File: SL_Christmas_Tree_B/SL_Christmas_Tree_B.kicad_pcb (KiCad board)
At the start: 2 copper layers, 85.7 x 116 mm, 60 parts

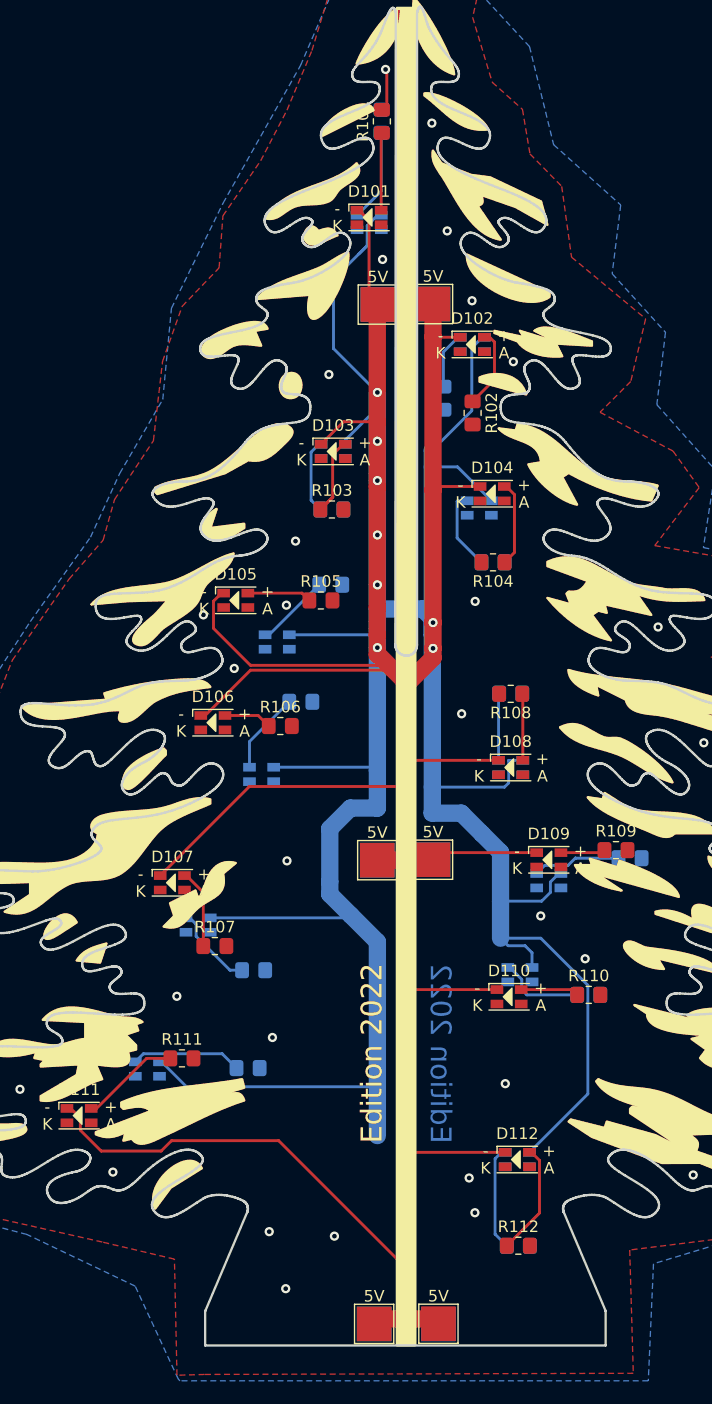
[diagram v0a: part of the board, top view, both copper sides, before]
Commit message: fix swapped 5V / GND
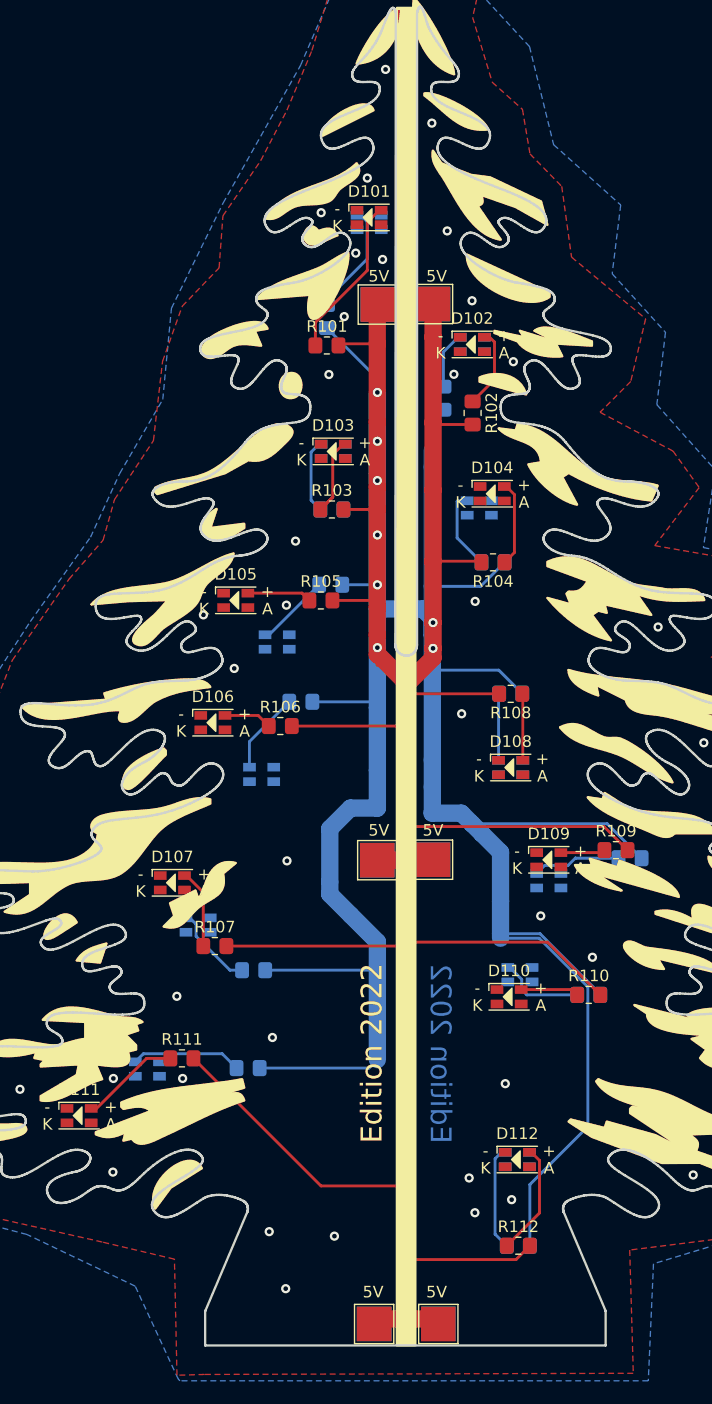
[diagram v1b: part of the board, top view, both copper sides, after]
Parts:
- 5V-101, 5V-102, 5V-201, 5V-202: renamed from GND; moved to F.Cu
- GND-101, GND-102, GND-201, GND-202: renamed from 5V; moved to B.Cu
- J101, J102: renamed from 5V; value 5V -> GND; moved to B.Cu
- J201, J202: renamed from GND; value GND -> 5V; moved to F.Cu
- moved R101 20.0 mm to (93.0, 79.0), turned to 0 degrees
- moved R201 17.6 mm to (93.0, 76.5), turned to -90 degrees
- turned 5V-101 to 0 degrees
- turned 5V-102 to 0 degrees
- turned 5V-201 to 0 degrees
- turned 5V-202 to 0 degrees
- turned GND-101 to 180 degrees
- turned GND-102 to 180 degrees
- turned GND-201 to 180 degrees
- turned GND-202 to 180 degrees
- turned J101 to 180 degrees
- turned J102 to 180 degrees
- turned J201 to 0 degrees
- turned J202 to 0 degrees
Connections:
- 5V-101 pad 1: GND -> +5V
- 5V-102 pad 1: GND -> +5V
- 5V-201 pad 1: GND -> +5V
- 5V-202 pad 1: GND -> +5V
- D101 pad 1: +5V -> GND
- D102 pad 1: +5V -> GND
- D103 pad 1: +5V -> GND
- D104 pad 1: +5V -> GND
- D105 pad 1: +5V -> GND
- D106 pad 1: +5V -> GND
- D107 pad 1: +5V -> GND
- D108 pad 1: +5V -> GND
- D109 pad 1: +5V -> GND
- D110 pad 1: +5V -> GND
- D111 pad 1: +5V -> GND
- D112 pad 1: +5V -> GND
- D201 pad 1: +5V -> GND
- D202 pad 1: +5V -> GND
- D203 pad 1: +5V -> GND
- D204 pad 1: +5V -> GND
- D205 pad 1: +5V -> GND
- D206 pad 1: +5V -> GND
- D207 pad 1: +5V -> GND
- D208 pad 1: +5V -> GND
- D209 pad 1: +5V -> GND
- D210 pad 1: +5V -> GND
- D211 pad 1: +5V -> GND
- D212 pad 1: +5V -> GND
- GND-101 pad 1: +5V -> GND
- GND-102 pad 1: +5V -> GND
- GND-201 pad 1: +5V -> GND
- GND-202 pad 1: +5V -> GND
- J101 pad 1: +5V -> GND
- J102 pad 1: +5V -> GND
- J201 pad 1: GND -> +5V
- J202 pad 1: GND -> +5V
- R101 pad 2: GND -> +5V
- R102 pad 2: GND -> +5V
- R103 pad 2: GND -> +5V
- R104 pad 2: GND -> +5V
- R105 pad 2: GND -> +5V
- R106 pad 2: GND -> +5V
- R107 pad 2: GND -> +5V
- R108 pad 2: GND -> +5V
- R109 pad 2: GND -> +5V
- R110 pad 2: GND -> +5V
- R111 pad 2: GND -> +5V
- R112 pad 2: GND -> +5V
- R201 pad 2: GND -> +5V
- R202 pad 2: GND -> +5V
- R203 pad 2: GND -> +5V
- R204 pad 2: GND -> +5V
- R205 pad 2: GND -> +5V
- R206 pad 2: GND -> +5V
- R207 pad 2: GND -> +5V
- R208 pad 2: GND -> +5V
- R209 pad 2: GND -> +5V
- R210 pad 2: GND -> +5V
- R211 pad 2: GND -> +5V
- R212 pad 2: GND -> +5V
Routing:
- net +5V: track 550.8 -> 504.3 mm
- net Net-(D101-Pad2): track 6.72 -> 14.2 mm
- net GND: track 6.07 -> 3.77 mm, vias 30 -> 38
- net Net-(D201-Pad2): track 8.03 -> 9.77 mm
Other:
- board text added: "5V"
- board text added: "GND"

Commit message: fix Routing
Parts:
- moved D201 1.37 mm to (95.4, 67.8)
- moved D101 0.90 mm to (95.8, 67.6)
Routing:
- net GND: track 3.77 -> 33.3 mm, vias 38 -> 58
- net Net-(D201-Pad2): track 9.77 -> 10.3 mm

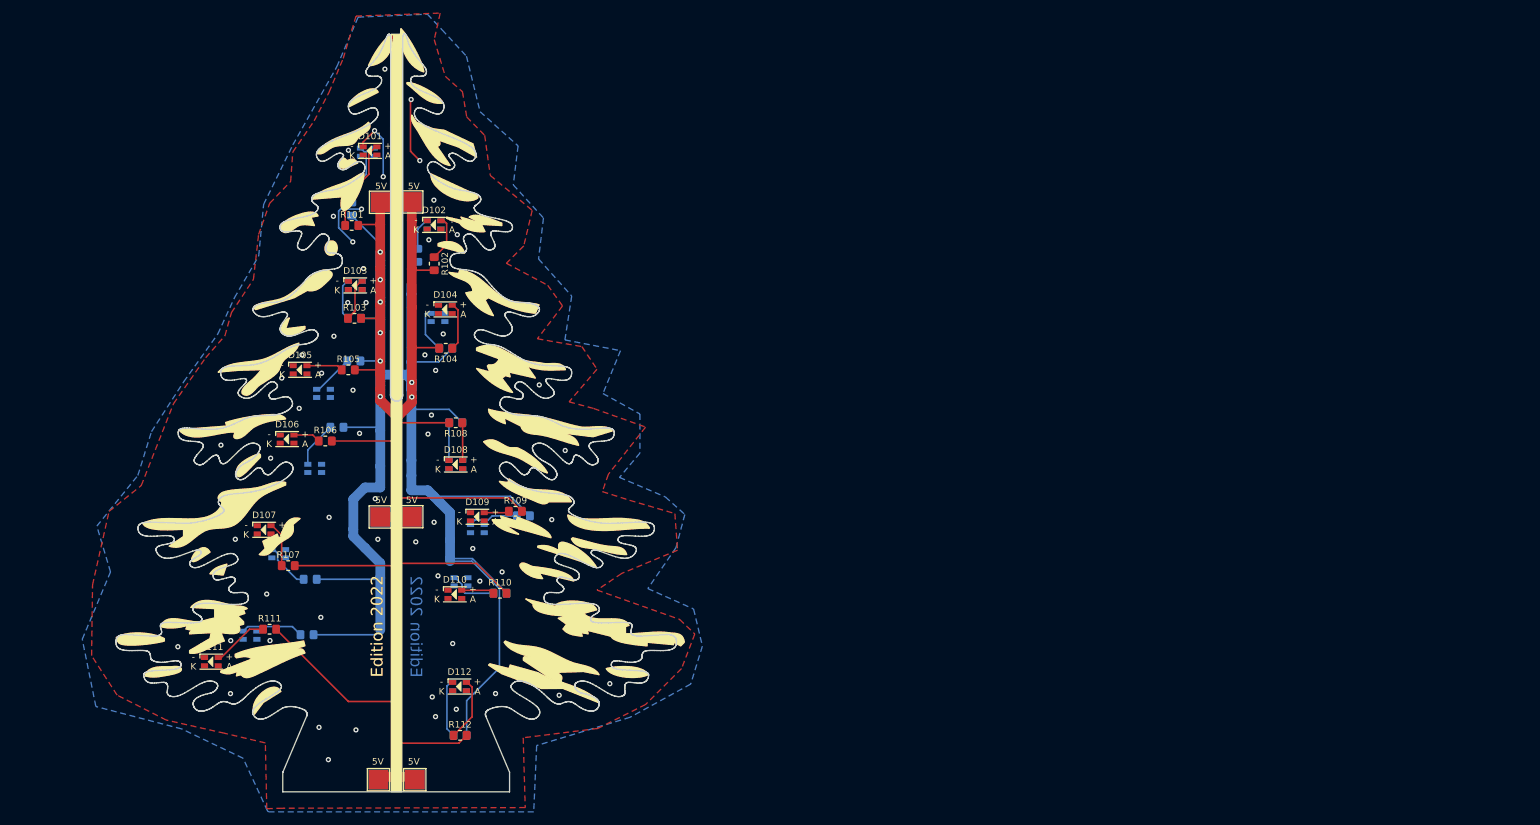
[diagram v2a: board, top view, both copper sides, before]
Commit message: small Footprint changes and prepared "Side B" for placing parts
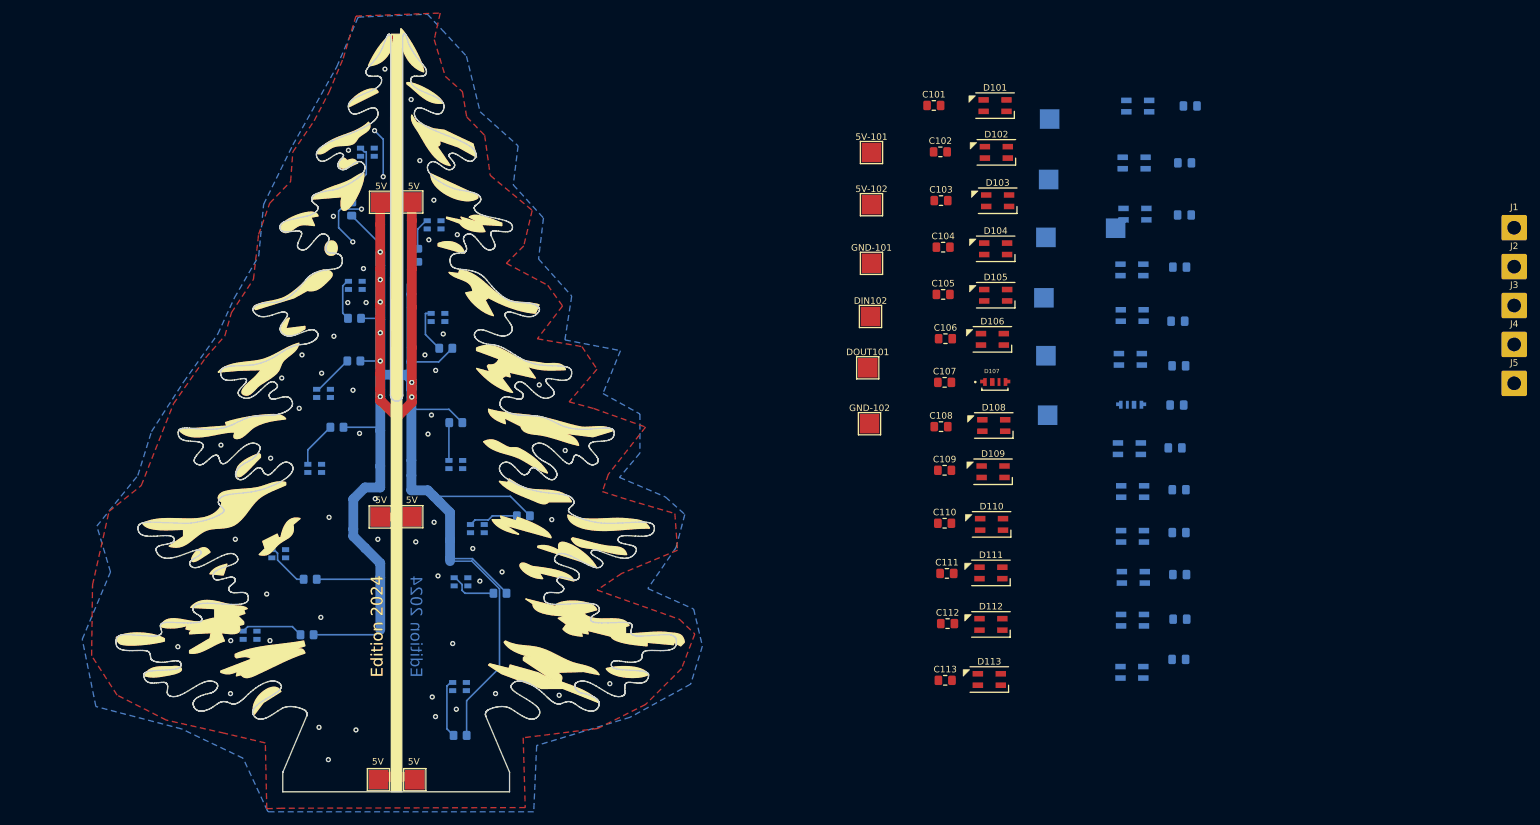
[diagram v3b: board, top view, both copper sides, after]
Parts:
- removed R101, R102, R103, R104, R105, R106, R107, R108, R109, R110, R111, R112: 200, Resistor_SMD:R_0805_2012Metric_Pad1.20x1.40mm_HandSolder
- added 5V-101: TestPoint, TestPoint:TestPoint_Pad_3.0x3.0mm, F.Cu at (172.5, 67.8)
- added 5V-102: TestPoint, TestPoint:TestPoint_Pad_3.0x3.0mm, F.Cu at (172.5, 75.8)
- added 5V-201: TestPoint, TestPoint:TestPoint_Pad_3.0x3.0mm, B.Cu at (199.8, 62.7)
- added 5V-202: TestPoint, TestPoint:TestPoint_Pad_3.0x3.0mm, B.Cu at (199.6, 72.0)
- added C101: 100nF, Capacitor_SMD:C_0805_2012Metric_Pad1.18x1.45mm_HandSolder, F.Cu at (182.0, 60.6)
- added C102: 100nF, Capacitor_SMD:C_0805_2012Metric_Pad1.18x1.45mm_HandSolder, F.Cu at (183.0, 67.8)
- added C103: 100nF, Capacitor_SMD:C_0805_2012Metric_Pad1.18x1.45mm_HandSolder, F.Cu at (183.1, 75.2)
- added C104: 100nF, Capacitor_SMD:C_0805_2012Metric_Pad1.18x1.45mm_HandSolder, F.Cu at (183.5, 82.3)
- added C105: 100nF, Capacitor_SMD:C_0805_2012Metric_Pad1.18x1.45mm_HandSolder, F.Cu at (183.5, 89.5)
- added C106: 100nF, Capacitor_SMD:C_0805_2012Metric_Pad1.18x1.45mm_HandSolder, F.Cu at (183.8, 96.3)
- added C107: 100nF, Capacitor_SMD:C_0805_2012Metric_Pad1.18x1.45mm_HandSolder, F.Cu at (183.7, 103.0)
- added C108: 100nF, Capacitor_SMD:C_0805_2012Metric_Pad1.18x1.45mm_HandSolder, F.Cu at (183.1, 109.8)
- added C109: 100nF, Capacitor_SMD:C_0805_2012Metric_Pad1.18x1.45mm_HandSolder, F.Cu at (183.7, 116.5)
- added C110: 100nF, Capacitor_SMD:C_0805_2012Metric_Pad1.18x1.45mm_HandSolder, F.Cu at (183.7, 124.5)
- added C111: 100nF, Capacitor_SMD:C_0805_2012Metric_Pad1.18x1.45mm_HandSolder, F.Cu at (184.0, 132.2)
- added C112: 100nF, Capacitor_SMD:C_0805_2012Metric_Pad1.18x1.45mm_HandSolder, F.Cu at (184.1, 139.9)
- added C113: 100nF, Capacitor_SMD:C_0805_2012Metric_Pad1.18x1.45mm_HandSolder, F.Cu at (183.8, 148.6)
- added C201: 100nF, Capacitor_SMD:C_0805_2012Metric_Pad1.18x1.45mm_HandSolder, B.Cu at (221.2, 60.7)
- added C202: 100nF, Capacitor_SMD:C_0805_2012Metric_Pad1.18x1.45mm_HandSolder, B.Cu at (220.4, 69.4)
- added C203: 100nF, Capacitor_SMD:C_0805_2012Metric_Pad1.18x1.45mm_HandSolder, B.Cu at (220.4, 77.4)
- added C204: 100nF, Capacitor_SMD:C_0805_2012Metric_Pad1.18x1.45mm_HandSolder, B.Cu at (219.6, 85.4)
- added C205: 100nF, Capacitor_SMD:C_0805_2012Metric_Pad1.18x1.45mm_HandSolder, B.Cu at (219.4, 93.7)
- added C206: 100nF, Capacitor_SMD:C_0805_2012Metric_Pad1.18x1.45mm_HandSolder, B.Cu at (219.5, 100.5)
- added C207: 100nF, Capacitor_SMD:C_0805_2012Metric_Pad1.18x1.45mm_HandSolder, B.Cu at (219.2, 106.5)
- added C208: 100nF, Capacitor_SMD:C_0805_2012Metric_Pad1.18x1.45mm_HandSolder, B.Cu at (218.9, 113.0)
- added C209: 100nF, Capacitor_SMD:C_0805_2012Metric_Pad1.18x1.45mm_HandSolder, B.Cu at (219.6, 119.4)
- added C210: 100nF, Capacitor_SMD:C_0805_2012Metric_Pad1.18x1.45mm_HandSolder, B.Cu at (219.6, 126.0)
- added C211: 100nF, Capacitor_SMD:C_0805_2012Metric_Pad1.18x1.45mm_HandSolder, B.Cu at (219.6, 132.4)
- added C212: 100nF, Capacitor_SMD:C_0805_2012Metric_Pad1.18x1.45mm_HandSolder, B.Cu at (219.7, 139.2)
- added C213: 100nF, Capacitor_SMD:C_0805_2012Metric_Pad1.18x1.45mm_HandSolder, B.Cu at (219.5, 145.4)
- added D113: SK6812MINI, parts:LED_SK6812MINI_PLCC4_3.5x3.5mm_P1.75mm, F.Cu at (190.5, 148.4)
- added D201: SK6812MINI, parts:LED_SK6812MINI_PLCC4_3.5x3.5mm_P1.75mm, B.Cu at (213.2, 60.8)
- added D202: SK6812MINI, parts:LED_SK6812MINI_PLCC4_3.5x3.5mm_P1.75mm, B.Cu at (212.7, 69.5)
- added D203: SK6812MINI, parts:LED_SK6812MINI_PLCC4_3.5x3.5mm_P1.75mm, B.Cu at (212.8, 77.3)
- added D204: SK6812MINI, parts:LED_SK6812MINI_PLCC4_3.5x3.5mm_P1.75mm, B.Cu at (212.3, 85.8)
- added D205: SK6812MINI, parts:LED_SK6812MINI_PLCC4_3.5x3.5mm_P1.75mm, B.Cu at (212.4, 92.8)
- added D206: SK6812MINI, parts:LED_SK6812MINI_PLCC4_3.5x3.5mm_P1.75mm, B.Cu at (212.1, 99.5)
- added D207: SK6812 4020, parts:LED_SK6812_4020, B.Cu at (212.3, 106.9)
- added D208: SK6812MINI, parts:LED_SK6812MINI_PLCC4_3.5x3.5mm_P1.75mm, B.Cu at (211.9, 113.2)
- added D209: SK6812MINI, parts:LED_SK6812MINI_PLCC4_3.5x3.5mm_P1.75mm, B.Cu at (212.4, 119.7)
- added D210: SK6812MINI, parts:LED_SK6812MINI_PLCC4_3.5x3.5mm_P1.75mm, B.Cu at (212.4, 126.5)
- added D211: SK6812MINI, parts:LED_SK6812MINI_PLCC4_3.5x3.5mm_P1.75mm, B.Cu at (212.6, 132.8)
- added D212: SK6812MINI, parts:LED_SK6812MINI_PLCC4_3.5x3.5mm_P1.75mm, B.Cu at (212.4, 139.4)
- added D213: SK6812MINI, parts:LED_SK6812MINI_PLCC4_3.5x3.5mm_P1.75mm, B.Cu at (212.3, 147.3)
- added DIN101: TestPoint, TestPoint:TestPoint_Pad_3.0x3.0mm, B.Cu at (209.8, 79.4)
- added DIN102: TestPoint, TestPoint:TestPoint_Pad_3.0x3.0mm, F.Cu at (172.3, 92.9)
- added DIN201: TestPoint, TestPoint:TestPoint_Pad_3.0x3.0mm, B.Cu at (199.2, 98.9)
- added DOUT101: TestPoint, TestPoint:TestPoint_Pad_3.0x3.0mm, F.Cu at (171.9, 100.8)
- added DOUT201: TestPoint, TestPoint:TestPoint_Pad_3.0x3.0mm, B.Cu at (199.4, 108.0)
- added GND-101: TestPoint, TestPoint:TestPoint_Pad_3.0x3.0mm, F.Cu at (172.5, 84.8)
- added GND-102: TestPoint, TestPoint:TestPoint_Pad_3.0x3.0mm, F.Cu at (172.2, 109.3)
- added GND-201: TestPoint, TestPoint:TestPoint_Pad_3.0x3.0mm, B.Cu at (199.2, 80.8)
- added GND-202: TestPoint, TestPoint:TestPoint_Pad_3.0x3.0mm, B.Cu at (198.9, 90.1)
- added J1: 5V, Connector_Wire:SolderWire-1.5sqmm_1x01_D1.7mm_OD3.9mm, F.Cu at (270.8, 79.3)
- added J2: DATA, Connector_Wire:SolderWire-1.5sqmm_1x01_D1.7mm_OD3.9mm, F.Cu at (270.8, 85.3)
- added J3: GND, Connector_Wire:SolderWire-1.5sqmm_1x01_D1.7mm_OD3.9mm, F.Cu at (270.8, 91.2)
- added J4: 5V, Connector_Wire:SolderWire-1.5sqmm_1x01_D1.7mm_OD3.9mm, F.Cu at (270.8, 97.2)
- added J5: GND, Connector_Wire:SolderWire-1.5sqmm_1x01_D1.7mm_OD3.9mm, F.Cu at (270.8, 103.2)
- D101, D102, D103, D104, D105, D106, D108, D109, D110, D111, D112: value LED -> SK6812MINI; footprint LED_SMD:LED_0807_Slow_Flashing_Diode -> parts:LED_SK6812MINI_PLCC4_3.5x3.5mm_P1.75mm
- D107: value LED -> SK6812 4020; footprint LED_SMD:LED_0807_Slow_Flashing_Diode -> parts:LED_SK6812_4020
- moved D111 120.0 mm to (190.8, 132.2)
- moved D107 113.9 mm to (191.4, 103.4)
- moved D106 108.9 mm to (191.0, 96.4)
- moved D105 107.0 mm to (191.5, 89.7)
- moved D103 99.1 mm to (191.8, 75.2)
- moved D101 95.9 mm to (191.4, 60.7)
- moved D102 86.7 mm to (191.6, 67.8)
- moved D104 84.7 mm to (191.5, 82.6)
- moved D110 82.8 mm to (190.9, 124.7)
- moved D108 82.5 mm to (191.2, 109.6)
- moved D112 81.8 mm to (190.8, 140.0)
- moved D109 79.2 mm to (191.1, 116.7)
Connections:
- D101 pad 1: GND -> Net-(D101-DOUT)
- D101 pad 2: Net-(D101-Pad2) -> GND
- D101 pad 3: (no net) -> Net-(D101-DIN)
- D101 pad 4: (no net) -> +5V
- D102 pad 1: GND -> Net-(D102-DOUT)
- D102 pad 2: Net-(D102-Pad2) -> GND
- D102 pad 3: (no net) -> Net-(D101-DOUT)
- D102 pad 4: (no net) -> +5V
- D103 pad 1: GND -> Net-(D103-DOUT)
- D103 pad 2: Net-(D103-Pad2) -> GND
- D103 pad 3: (no net) -> Net-(D102-DOUT)
- D103 pad 4: (no net) -> +5V
- D104 pad 1: GND -> Net-(D104-DOUT)
- D104 pad 2: Net-(D104-Pad2) -> GND
- D104 pad 3: (no net) -> Net-(D103-DOUT)
- D104 pad 4: (no net) -> +5V
- D105 pad 1: GND -> Net-(D105-DOUT)
- D105 pad 2: Net-(D105-Pad2) -> GND
- D105 pad 3: (no net) -> Net-(D104-DOUT)
- D105 pad 4: (no net) -> +5V
- D106 pad 1: GND -> Net-(D106-DOUT)
- D106 pad 2: Net-(D106-Pad2) -> GND
- D106 pad 3: (no net) -> Net-(D105-DOUT)
- D106 pad 4: (no net) -> +5V
- D107 pad 1: GND -> Net-(D106-DOUT)
- D107 pad 2: Net-(D107-Pad2) -> +5V
- D107 pad 3: (no net) -> Net-(D107-DOUT)
- D107 pad 4: (no net) -> GND
- D108 pad 1: GND -> Net-(D108-DOUT)
- D108 pad 2: Net-(D108-Pad2) -> GND
- D108 pad 3: (no net) -> Net-(D108-DIN)
- D108 pad 4: (no net) -> +5V
- D109 pad 1: GND -> Net-(D109-DOUT)
- D109 pad 2: Net-(D109-Pad2) -> GND
- D109 pad 3: (no net) -> Net-(D108-DOUT)
- D109 pad 4: (no net) -> +5V
- D110 pad 1: GND -> Net-(D110-DOUT)
- D110 pad 2: Net-(D110-Pad2) -> GND
- D110 pad 3: (no net) -> Net-(D109-DOUT)
- D110 pad 4: (no net) -> +5V
- D111 pad 1: GND -> Net-(D111-DOUT)
- D111 pad 2: Net-(D111-Pad2) -> GND
- D111 pad 3: (no net) -> Net-(D110-DOUT)
- D111 pad 4: (no net) -> +5V
- D112 pad 1: GND -> Net-(D112-DOUT)
- D112 pad 2: Net-(D112-Pad2) -> GND
- D112 pad 3: (no net) -> Net-(D111-DOUT)
- D112 pad 4: (no net) -> +5V
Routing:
- net +5V: track 504.3 -> 379.8 mm
- net Net-(D101-Pad2): track 14.1 -> 0.00 mm
- net GND: track 33.3 -> 19.2 mm
- net Net-(D112-Pad2): track 9.73 -> 0.00 mm
- net Net-(D111-Pad2): track 8.66 -> 0.00 mm
- net Net-(D103-Pad2): track 8.20 -> 0.00 mm
- net Net-(D104-Pad2): track 7.39 -> 0.00 mm
- net Net-(D102-Pad2): track 6.98 -> 0.00 mm
- net Net-(D107-Pad2): track 6.88 -> 0.00 mm
- net Net-(D108-Pad2): track 5.78 -> 0.00 mm
- net Net-(D105-Pad2): track 5.59 -> 0.00 mm
- net Net-(D110-Pad2): track 5.04 -> 0.00 mm
- net Net-(D106-Pad2): track 4.17 -> 0.00 mm
- net Net-(D109-Pad2): track 3.86 -> 0.00 mm
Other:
- board text added: "Edition 2024"
- board text removed: "Edition 2022"

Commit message: some layout fixes
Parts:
- removed the D201 at (95.4, 67.8)
- removed the D202 at (105.6, 78.9)
- removed the D203 at (93.5, 88.2)
- removed the D204 at (106.2, 93.1)
- removed the D205 at (88.7, 104.7)
- removed the D206 at (87.3, 116.2)
- removed the D207 at (81.8, 129.2)
- removed the D208 at (108.9, 115.6)
- removed the D209 at (112.2, 125.4)
- removed the D210 at (109.7, 133.5)
- removed the D211 at (77.5, 141.7)
- removed the D212 at (109.5, 149.5)
- removed R201, R202, R203, R204, R205, R206, R207, R208, R209, R210, R211, R212: 200, Resistor_SMD:R_0805_2012Metric_Pad1.20x1.40mm_HandSolder
- moved J101 0.41 mm to (97.5, 163.8)
- moved J202 0.40 mm to (102.2, 163.8)
- moved J102 0.38 mm to (102.3, 163.8)
- moved J201 0.36 mm to (97.5, 163.8)
- moved 5V-101 0.11 mm to (97.5, 123.6)
- moved GND-101 0.11 mm to (97.5, 123.6)
- moved 5V-202 0.06 mm to (102.2, 123.5)
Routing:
- net +5V: track 379.8 -> 258.3 mm
- net GND: track 19.2 -> 1.99 mm
- net Net-(D201-Pad2): track 10.3 -> 0.00 mm
- net Net-(D211-Pad2): track 9.57 -> 0.00 mm
- net Net-(D212-Pad2): track 9.07 -> 0.00 mm
- net Net-(D209-Pad2): track 7.66 -> 0.00 mm
- net Net-(D210-Pad2): track 7.52 -> 0.00 mm
- net Net-(D207-Pad2): track 7.35 -> 0.00 mm
- net Net-(D206-Pad2): track 7.09 -> 0.00 mm
- net Net-(D204-Pad2): track 7.06 -> 0.00 mm
- net Net-(D205-Pad2): track 6.49 -> 0.00 mm
- net Net-(D203-Pad2): track 6.46 -> 0.00 mm
- net Net-(D208-Pad2): track 5.81 -> 0.00 mm
- net Net-(D202-Pad2): track 5.17 -> 0.00 mm
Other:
- outline, holes or cut-outs redrawn

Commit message: WIP v2.1
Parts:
- removed 5V-101, 5V-102, 5V-201, 5V-202, DIN102, DOUT101, GND-101, GND-102, GND-201, GND-202: TestPoint, TestPoint:TestPoint_Pad_3.0x3.0mm
- removed C107, C207: 100nF, Capacitor_SMD:C_0805_2012Metric_Pad1.18x1.45mm_HandSolder
- removed D107, D207: SK6812 4020, parts:LED_SK6812_4020
- removed J1, J4: 5V, Connector_Wire:SolderWire-1.5sqmm_1x01_D1.7mm_OD3.9mm
- removed J101, J102: GND, TestPoint:TestPoint_Pad_3.0x3.0mm
- removed J2: DATA, Connector_Wire:SolderWire-1.5sqmm_1x01_D1.7mm_OD3.9mm
- removed J201, J202: 5V, TestPoint:TestPoint_Pad_3.0x3.0mm
- removed J3, J5: GND, Connector_Wire:SolderWire-1.5sqmm_1x01_D1.7mm_OD3.9mm
- added 5V: TestPoint, TestPoint:TestPoint_Pad_3.0x3.0mm, F.Cu at (102.3, 75.5)
- added 5V: TestPoint, TestPoint:TestPoint_Pad_3.0x3.0mm, F.Cu at (97.4, 75.5)
- added DT: TestPoint, TestPoint:TestPoint_Pad_3.0x3.0mm, F.Cu at (98.0, 61.7)
- added GND: TestPoint, TestPoint:TestPoint_Pad_3.0x3.0mm, B.Cu at (102.3, 75.5)
- added GND: TestPoint, TestPoint:TestPoint_Pad_3.0x3.0mm, B.Cu at (97.3, 75.5)
- 5V: renamed from 5V-202; moved to F.Cu
- 5V: renamed from 5V-201; moved to F.Cu
- DT: renamed from DIN101; moved to F.Cu
- GND: renamed from GND-102; moved to B.Cu
- GND: renamed from GND-101; moved to B.Cu
- moved C213 176.8 mm to (42.8, 150.4)
- moved C212 174.3 mm to (45.7, 128.1)
- moved C211 168.8 mm to (52.4, 109.8)
- moved C210 162.7 mm to (60.6, 91.2)
- moved C209 161.0 mm to (65.0, 74.4)
- moved C208 156.8 mm to (71.7, 59.0)
- moved C201 134.6 mm to (139.8, 167.9)
- moved D212 132.3 mm to (80.1, 139.5)
- moved D210 128.4 mm to (85.0, 110.8)
- moved D211 125.5 mm to (87.1, 129.1)
- moved D209 125.3 mm to (88.8, 99.6)
- moved D201 124.7 mm to (122.1, 145.8)
- moved D202 124.4 mm to (108.6, 137.5)
- moved D208 121.9 mm to (92.3, 89.5)
- moved D213 121.3 mm to (91.0, 148.5)
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- renumbered 5V-101 to 5V, 5V-102 to 5V, DIN201 to DT, DOUT201 to DT, GND-201 to GND, GND-202 to GND
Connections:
- D106 pad 1: Net-(D106-DOUT) -> Conn_A-OUT_B-IN
- D108 pad 3: Net-(D108-DIN) -> Conn_B-OUT_A-IN
- D113 pad 1: Conn_A-OUT_B-IN -> Net-(D113-DOUT)
- D213 pad 1: unconnected-(D213-DOUT-Pad1) -> Conn_B-OUT_A-IN
- DT pad 1: Net-(D207-DOUT) -> Net-(D206-DOUT)
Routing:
- net +5V: track 258.3 -> 263.9 mm
- net GND: track 1.99 -> 0.28 mm
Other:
- outline, holes or cut-outs redrawn
- board text removed: "5V"
- board text removed: "GND"
